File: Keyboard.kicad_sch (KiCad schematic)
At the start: 13 parts, among them J1 USB_C_Receptacle, J2 Conn_02x01_Row_Letter_First, U1 ESP32-C3FH4, U3 MCP73831-2-OT

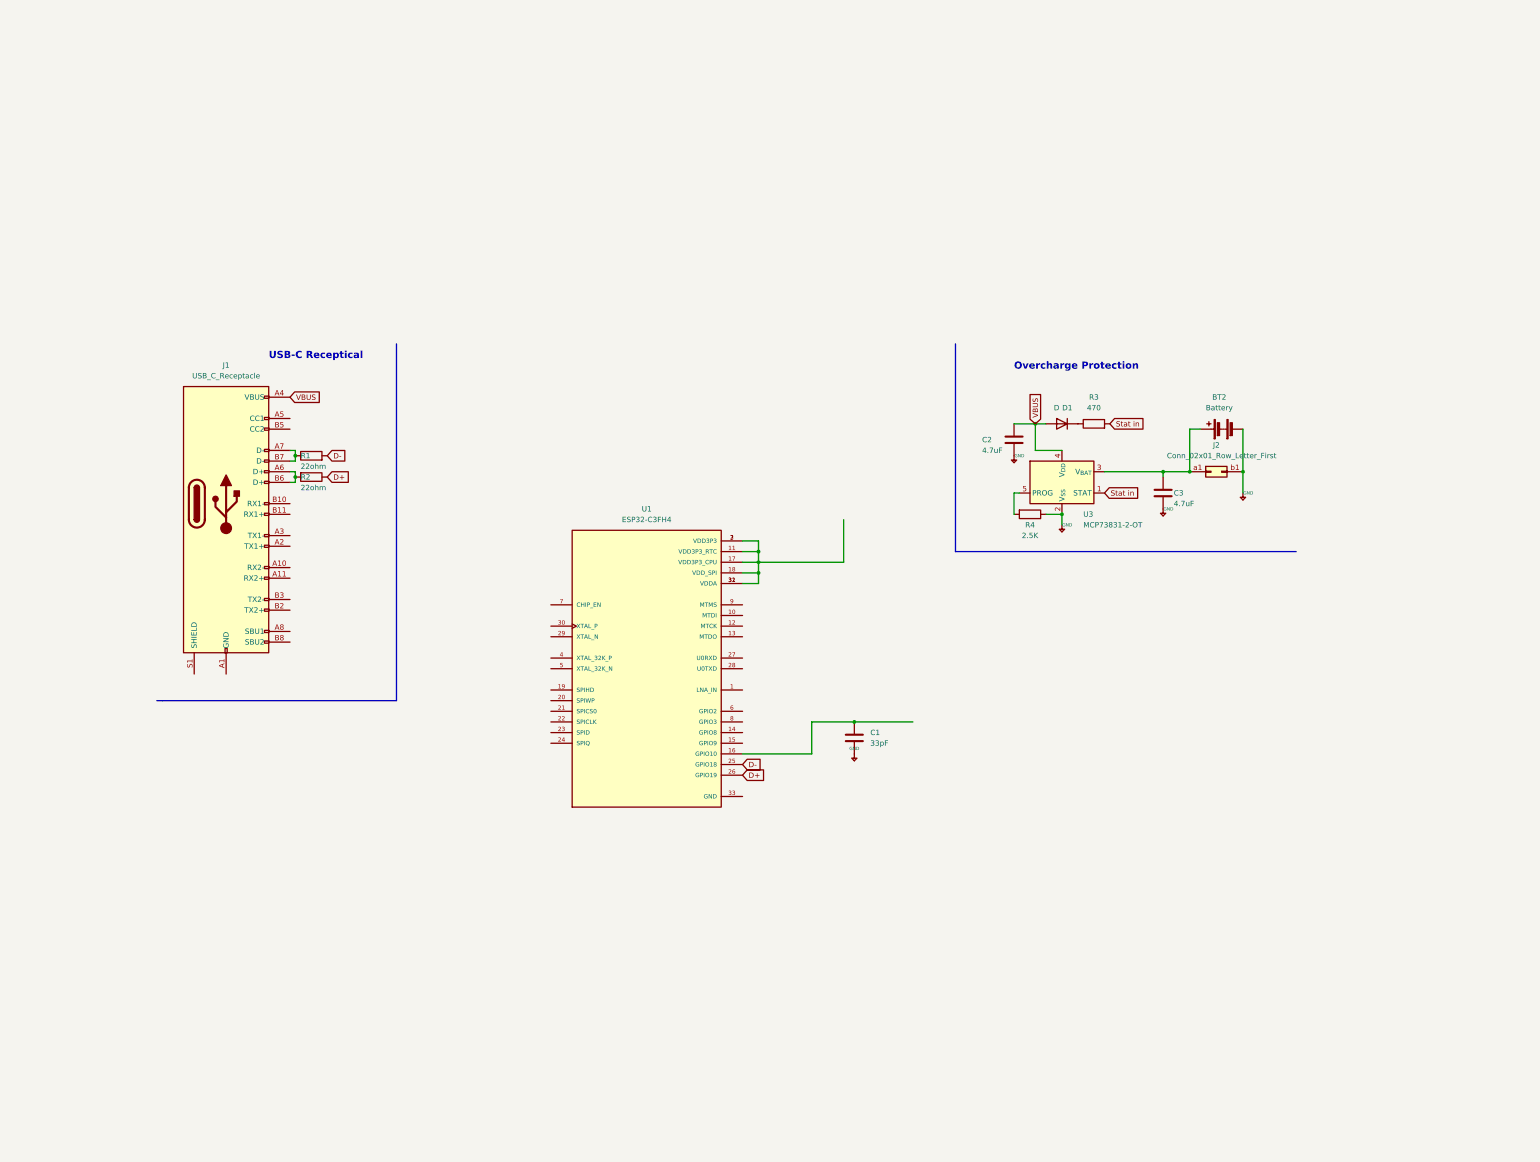
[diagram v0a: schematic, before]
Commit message: finished keyboard matrix, worked on LED backlight
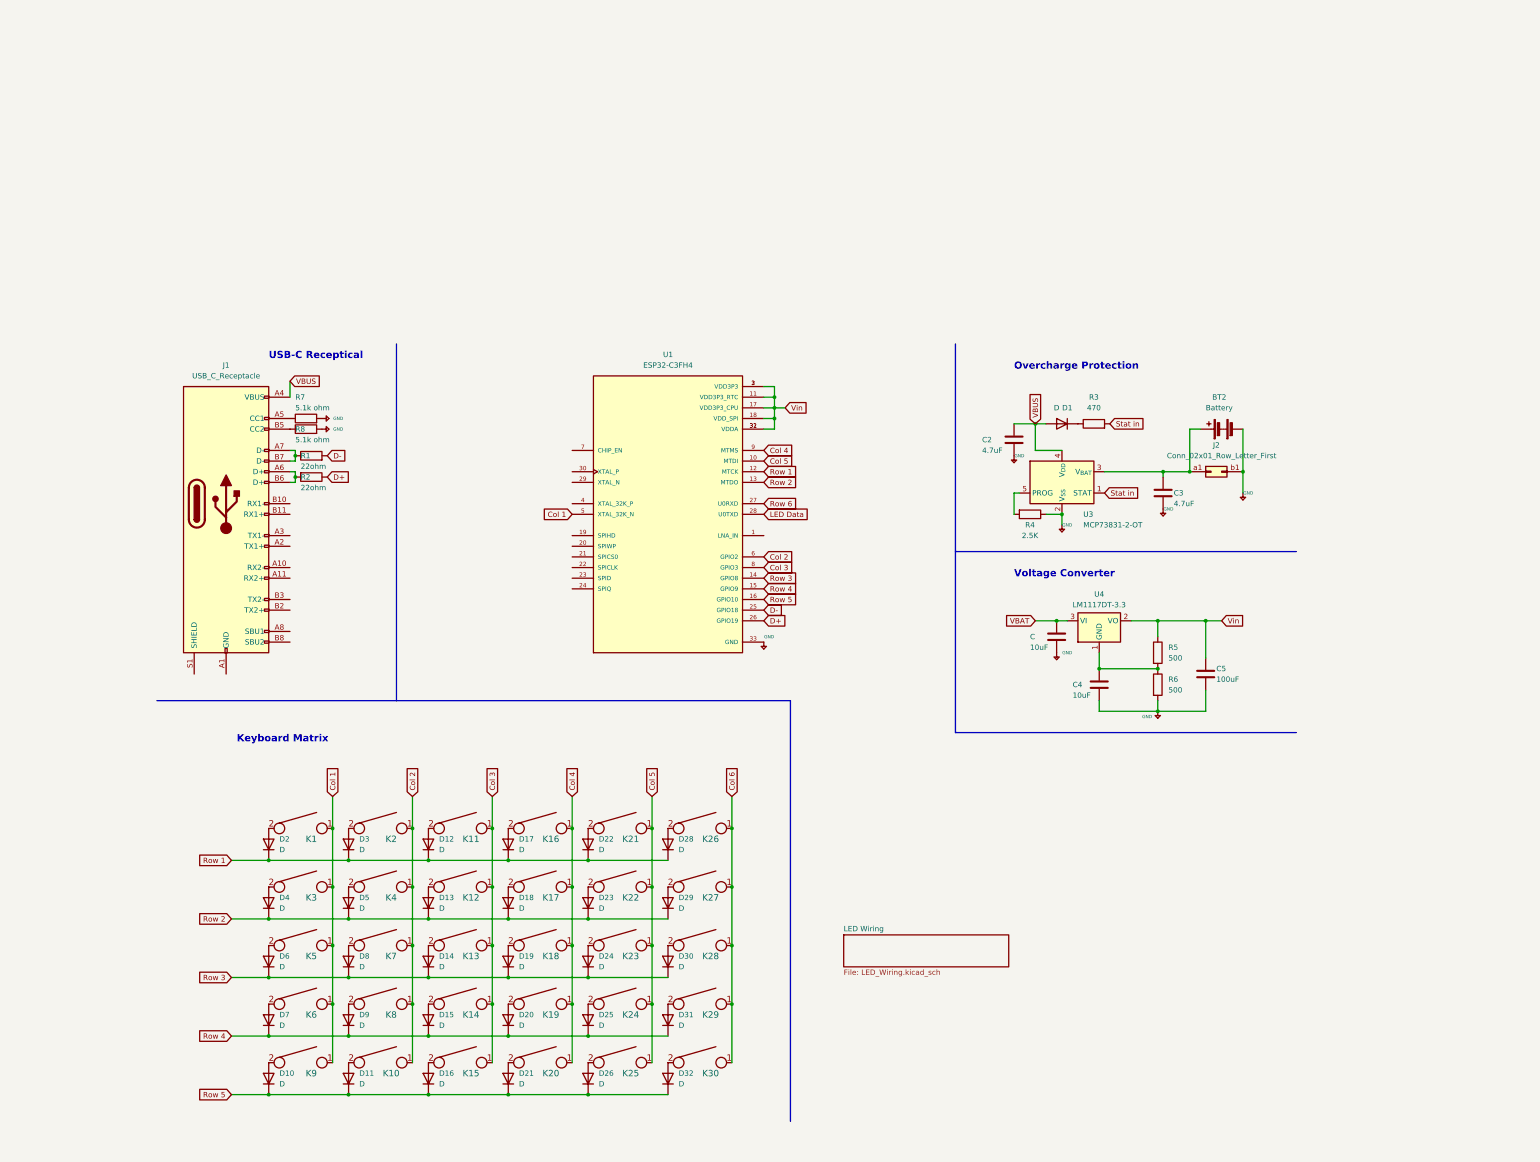
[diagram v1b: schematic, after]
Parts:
- removed C1: 33pF, symbol Device:C
- added C, C4: 10uF, symbol Device:C
- added C5: 100uF, symbol Device:C
- added D10, D11, D12, D13, D14, D15, D16, D17, D18, D19, D2, D20, D21, D22, D23, D24, D25, D26, D28, D29, D3, D30, D31, D32, D4, D5, D6, D7, D8, D9: D, symbol Device:D
- added K1, K10, K11, K12, K13, K14, K15, K16, K17, K18, K19, K2, K20, K21, K22, K23, K24, K25, K26, K27, K28, K29, K3, K30, K4, K5, K6, K7, K8, K9: KEYSW, symbol keyboard_parts2:KEYSW
- added R5, R6: 500, symbol Device:R
- added R7, R8: 5.1k ohm, symbol Device:R
- added U4: LM1117DT-3.3, Package_TO_SOT_SMD:TO-252-3_TabPin2, symbol Regulator_Linear:LM1117DT-3.3
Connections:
- net +5V: now also U1.33 (GND), C.2, C4.2, C5.2, R6.2, R7.2, R8.2
- net Col 5: now reaches U1.10 (MTDI)
- net Col 5: now also K21.1, K22.1, K23.1, K24.1, K25.1
- net Vin: now reaches U1.11 (VDD3P3_RTC), U1.17 (VDD3P3_CPU), U1.18 (VDD_SPI), U1.2 (VDD3P3), U1.3 (VDD3P3), U1.31 (VDDA), U1.32 (VDDA)
- net Vin: now also C5.1, R5.1, U4.2 (VO)
- net Row 1: now reaches U1.12 (MTCK)
- net Row 1: now also D12.1 (K), D17.1 (K), D2.1 (K), D22.1 (K), D28.1 (K), D3.1 (K)
- net Row 2: now reaches U1.13 (MTDO)
- net Row 2: now also D13.1 (K), D18.1 (K), D23.1 (K), D29.1 (K), D4.1 (K), D5.1 (K)
- net Row 3: now reaches U1.14 (GPIO8)
- net Row 3: now also D14.1 (K), D19.1 (K), D24.1 (K), D30.1 (K), D6.1 (K), D8.1 (K)
- net Row 4: now reaches U1.15 (GPIO9)
- net Row 4: now also D15.1 (K), D20.1 (K), D25.1 (K), D31.1 (K), D7.1 (K), D9.1 (K)
- net Row 5: now reaches U1.16 (GPIO10)
- net Row 5: now also D10.1 (K), D11.1 (K), D16.1 (K), D21.1 (K), D26.1 (K), D32.1 (K)
- net Row 6: now reaches U1.27 (U0RXD)
- net LED Data: now reaches U1.28 (U0TXD)
- net Col 1: now reaches U1.5 (XTAL_32K_N)
- net Col 1: now also K1.1, K3.1, K5.1, K6.1, K9.1
- net Col 2: now reaches U1.6 (GPIO2)
- net Col 2: now also K10.1, K2.1, K4.1, K7.1, K8.1
- net Col 3: now reaches U1.8 (GPIO3)
- net Col 3: now also K11.1, K12.1, K13.1, K14.1, K15.1
- net Col 4: now reaches U1.9 (MTMS)
- net Col 4: now also K16.1, K17.1, K18.1, K19.1, K20.1
- net at J1.A5 (CC1): now also R7.1
- net at J1.B5 (CC2): now also R8.1
- new net: D6.2 (A), K5.2
- new net: D14.2 (A), K13.2
- new net: D12.2 (A), K11.2
- new net: D28.2 (A), K26.2
- new net: D25.2 (A), K24.2
- new net: D8.2 (A), K7.2
- new net: D7.2 (A), K6.2
- new net: D24.2 (A), K23.2
- new net: D29.2 (A), K27.2
- new net: D10.2 (A), K9.2
- new net: D21.2 (A), K20.2
- new net: D2.2 (A), K1.2
- new net: D31.2 (A), K29.2
- new net: C4.1, R5.2, R6.1, U4.1 (GND)
- new net: D17.2 (A), K16.2
- new net: D11.2 (A), K10.2
- new net: D9.2 (A), K8.2
- new net: D20.2 (A), K19.2
- new net: D13.2 (A), K12.2
- new net: D16.2 (A), K15.2
- new net: D22.2 (A), K21.2
- new net: D32.2 (A), K30.2
- new net: D15.2 (A), K14.2
- new net: D4.2 (A), K3.2
- new net: D5.2 (A), K4.2
- new net: D26.2 (A), K25.2
- new net: D30.2 (A), K28.2
- new net: D3.2 (A), K2.2
- new net: D23.2 (A), K22.2
- new net: D18.2 (A), K17.2
- new net: D19.2 (A), K18.2
- new net Col 6: K26.1, K27.1, K28.1, K29.1, K30.1
- new net VBAT: C.1, U4.3 (VI)
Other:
- added sheet LED Wiring (LED_Wiring.kicad_sch)
- note added: "Keyboard Matrix"
- note added: "Voltage Converter"
- moved on the sheet: U1

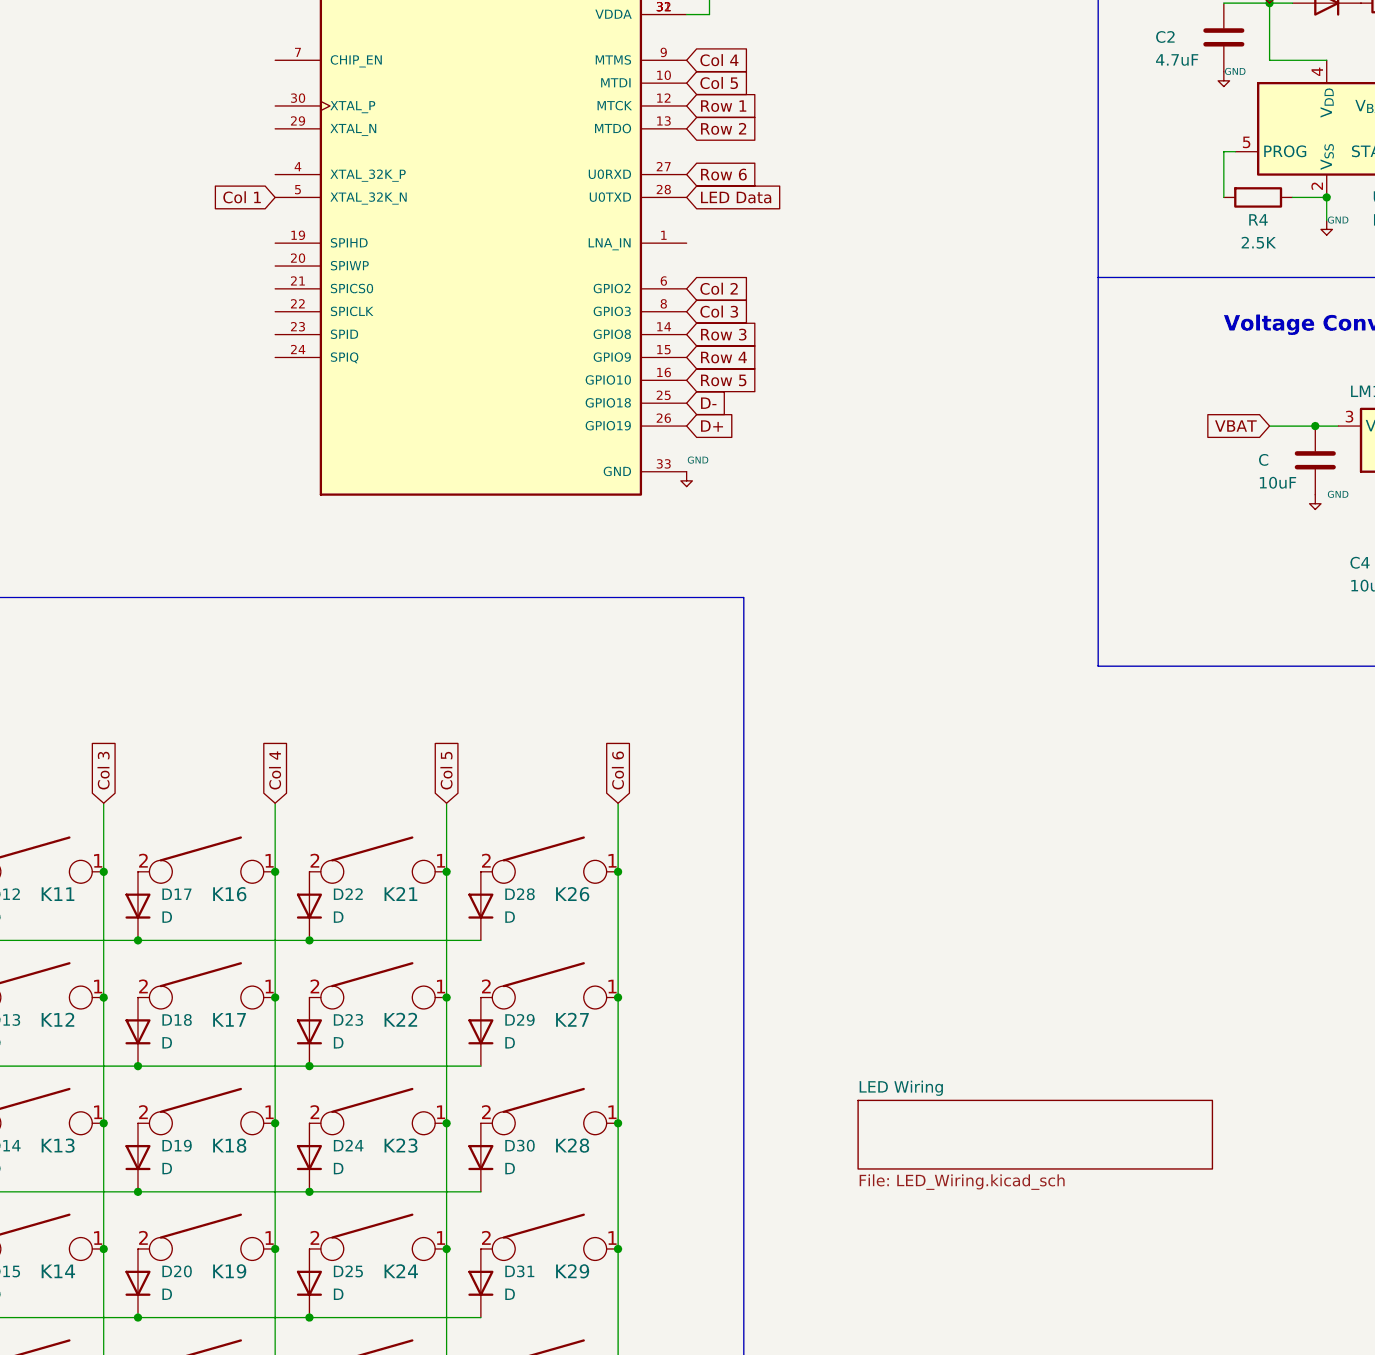
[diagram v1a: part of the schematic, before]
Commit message: bare bones of the keyboard complete
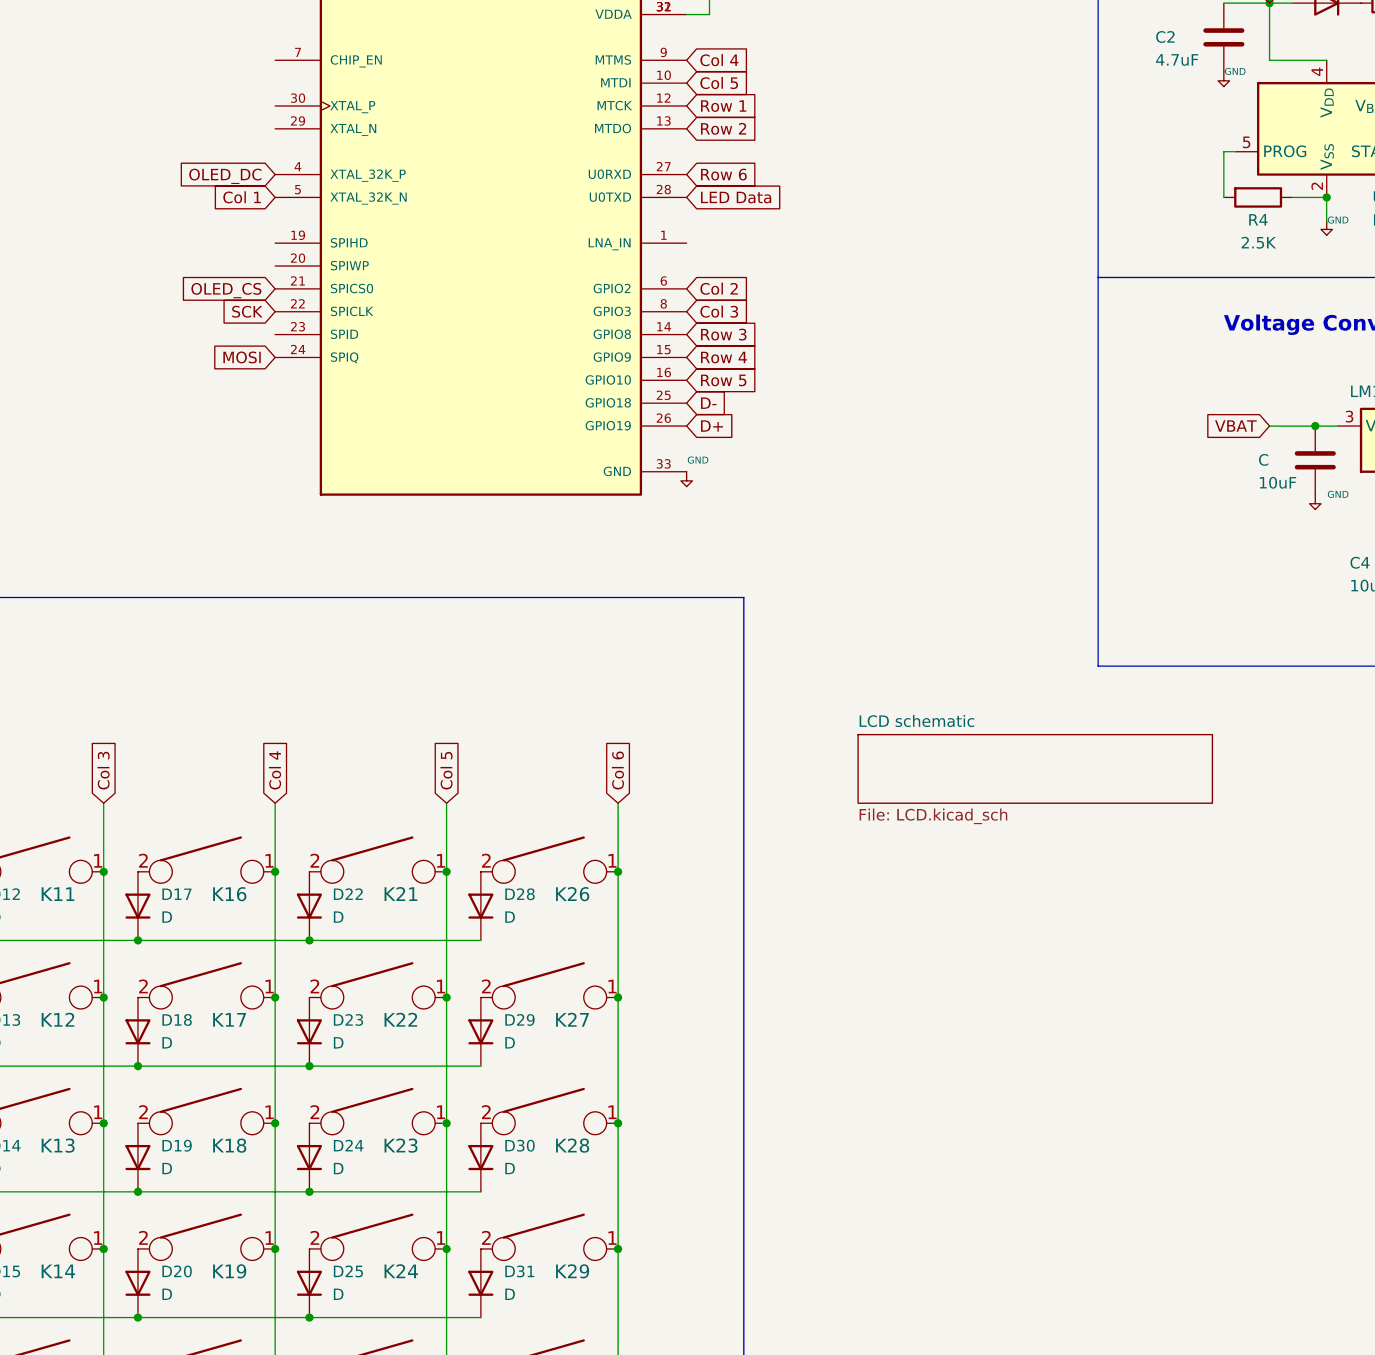
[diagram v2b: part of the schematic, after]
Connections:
- net OLED_CS: now reaches U1.21 (SPICS0)
- net SCK: now reaches U1.22 (SPICLK)
- net MOSI: now reaches U1.24 (SPIQ)
- net OLED_DC: now reaches U1.4 (XTAL_32K_P)
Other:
- removed sheet LED Wiring
- added sheet LCD schematic (LCD.kicad_sch)
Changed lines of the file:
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@@
+    )
+  )
+  (global_label "SCK" (shape input) (at 111.76 66.04 180) (fields_autoplaced)
+    (effects (font (size 1.27 1.27)) (justify right))
+    (property "Intersheetrefs" "${INTERSHEET_REFS}" (at 105.0253 66.04 0)
+      (effects (font (size 1.27 1.27)) (justify right) hide)
     )
   )
@@
     )
   )
+  (global_label "MOSI" (shape input) (at 111.76 71.12 180) (fields_autoplaced)
+    (effects (font (size 1.27 1.27)) (justify right))
+    (property "Intersheetrefs" "${INTERSHEET_REFS}" (at 104.1786 71.12 0)
+      (effects (font (size 1.27 1.27)) (justify right) hide)
+    )
+  )
   (global_label "Row 3" (shape input) (at 30.48 163.83 180) (fields_autoplaced)
     (effects (font (size 1.27 1.27)) (justify right))
@@
     )
   )
+  (global_label "OLED_CS" (shape input) (at 111.76 63.5 180) (fields_autoplaced)
+    (effects (font (size 1.27 1.27)) (justify right))
+    (property "Intersheetrefs" "${INTERSHEET_REFS}" (at 100.5501 63.5 0)
+      (effects (font (size 1.27 1.27)) (justify right) hide)
+    )
+  )
   (global_label "Col 1" (shape input) (at 111.76 53.34 180) (fields_autoplaced)
     (effects (font (size 1.27 1.27)) (justify right))
     (property "Intersheetrefs" "${INTERSHEET_REFS}" (at 103.5135 53.34 0)
+      (effects (font (size 1.27 1.27)) (justify right) hide)
+    )
+  )
+  (global_label "OLED_DC" (shape input) (at 111.76 50.8 180) (fields_autoplaced)
+    (effects (font (size 1.27 1.27)) (justify right))
+    (property "Intersheetrefs" "${INTERSHEET_REFS}" (at 100.4896 50.8 0)
       (effects (font (size 1.27 1.27)) (justify right) hide)
     )
@@
     )
   )
-  (sheet (at 176.53 153.67) (size 39.37 7.62) (fields_autoplaced)
+  (sheet (at 176.53 113.03) (size 39.37 7.62) (fields_autoplaced)
     (stroke (width 0.1524) (type solid))
-    (fill (color 92 255 95 1.0000))
-    (property "Sheetname" "LED Wiring" (at 176.53 152.9584 0)
+    (fill (color 68 247 255 1.0000))
+    (property "Sheetname" "LCD schematic" (at 176.53 112.3184 0)
       (effects (font (size 1.27 1.27)) (justify left bottom))
     )
-    (property "Sheetfile" "LED_Wiring.kicad_sch" (at 176.53 161.8746 0)
+    (property "Sheetfile" "LCD.kicad_sch" (at 176.53 121.2346 0)
       (effects (font (size 1.27 1.27)) (justify left top))
     )
     (instances
       (project "Keyboard"
-        (path "/0c6e22c2-b00a-47ce-bc43-0c577bef5c57" (page "2"))
-      )
-    )
+        (path "/0c6e22c2-b00a-47ce-bc43-0c577bef5c57" (page "3"))
+      )
+    )
